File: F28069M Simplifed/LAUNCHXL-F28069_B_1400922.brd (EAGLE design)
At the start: 130.6 x 51.1 mm, 54 parts, among them U1 TMS320F28069MPZT, U10 SN74LV4052APW, U11 TS5A3153DCUR, U13 SN74AHC1G32, U14 SN74AHC1G32, U15 TS5A3153DCUR, U16 TS5A23159DGSR, U18 SN74LVC1G04DCKR, U4 SN74AHC1G02DBVR

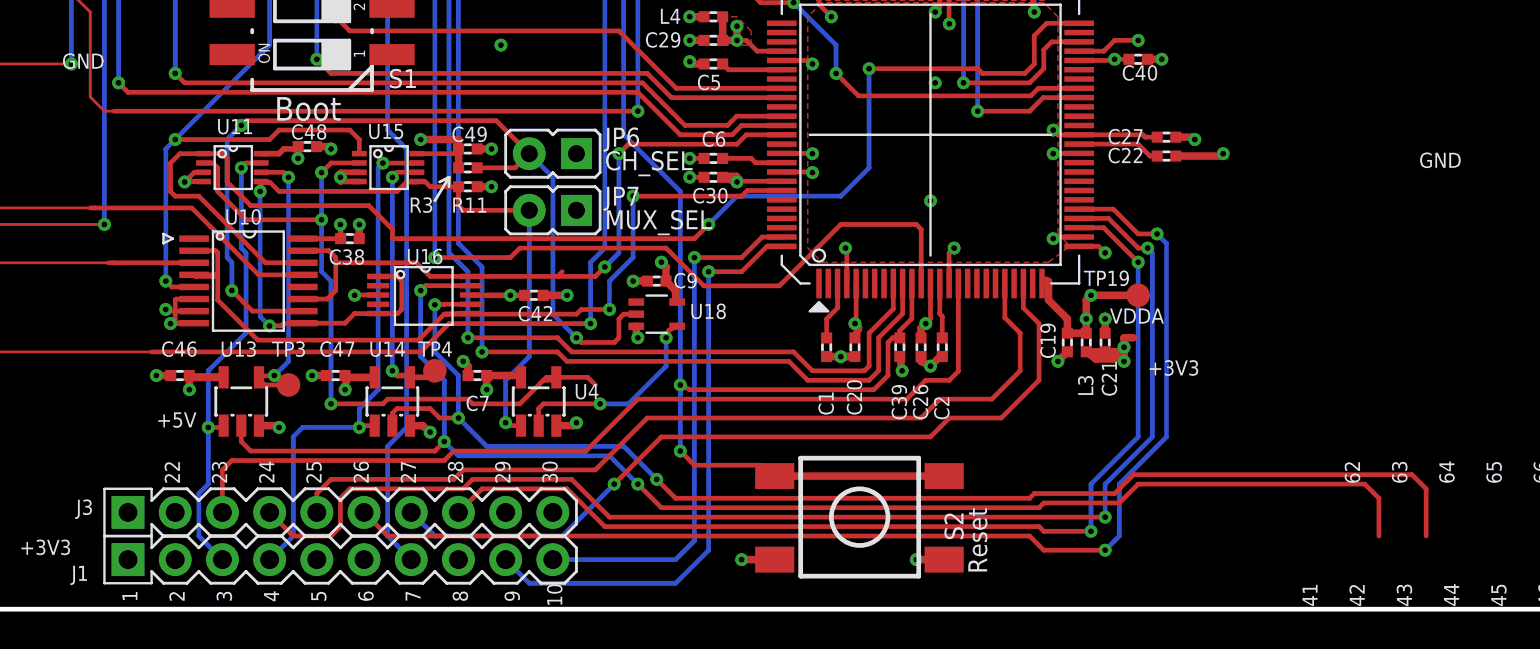
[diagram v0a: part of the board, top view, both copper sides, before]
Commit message: Final simplification of TI's F28069M microcontroller
Decided to remove all muxes and logic gates and make direct connection to GPIO 28 and 29 pins. No need to use their other functionality, serial TX and RX. We believe those serial lines are not involved when identifing a motor or flashing the microcontroller. We also decided on just one switch on TRST signal. The state of that line should decide whether code is automatically run on power up or if code is being flashed.
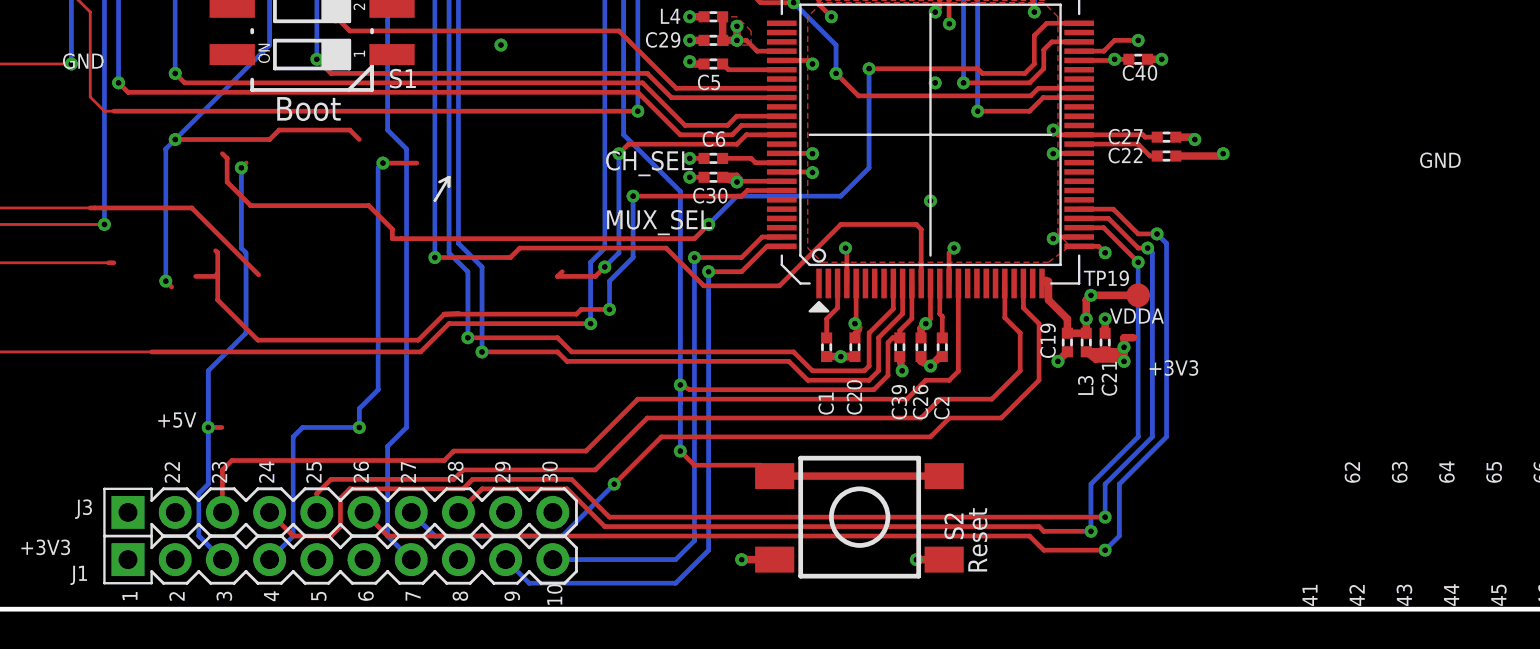
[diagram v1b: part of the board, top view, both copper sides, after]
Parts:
- removed C38, C42, C46, C47, C48, C49, C7, C9: 0.1u, rcl:C0402
- removed JP6, JP7: (no value), jumper:JP1
- removed R11, R3: 10K, rcl:R0402
- removed TP3, TP4: TESTPAD_TPB1,27, RF430FRL152H_EVM_a:TESTPAD_B1,27
- removed U10: SN74LV4052APW, LAUNCHXL-F28027:TSSOP16-PW
- removed U11, U15: TS5A3153DCUR, LAUNCHXL-F28027:TI-DCU8
- removed U13, U14: SN74AHC1G32, LAUNCHXL-F28027:SOT23-5-DBV
- removed U16: TS5A23159DGSR, LAUNCHXL-F28027:TI-DGS10
- removed U18: SN74LVC1G04DCKR, RF430FRL152H_EVM_a:74XX-LITTLE-DE_SC70-5
- removed U4: SN74AHC1G02DBVR, LAUNCHXL-F28027:SOT23-5-DBV
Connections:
- removed net !EN: U11.P$2, U15.P$2, U4.4
- removed net CH_SEL: JP6.2, R3.2, U10.P$10, U18.2
- removed net FAULT_O: TP3.TP, U11.P$6, U13.4
- removed net J7.3: U13.2, U16.P$9
- removed net J7.4: U14.2, U16.P$7
- removed net MUX_SEL: JP7.2, R11.2, U10.P$9, U11.P$5, U15.P$5, U16.P$1, U16.P$5, U4.1
- removed net N$10: S1.5
- removed net N$42: U18.4, U4.2
- removed net OCTW_O: TP4.TP, U14.4, U15.P$6
- net +3V3: no longer C38.1, C42.1, C46.1, C47.1, C48.1, C49.1, C7.1, C9.1, R11.1, R3.1, U10.P$16, U11.P$8, U13.5, U14.5, U15.P$8, U16.P$8, U18.5, U4.5
- net GND: no longer C38.2, C42.2, C46.2, C47.2, C48.2, C49.2, C7.2, C9.2, JP6.1, JP7.1, U10.P$6, U10.P$7, U10.P$8, U11.P$3, U11.P$4, U13.3, U14.3, U15.P$3, U15.P$4, U16.P$3, U18.3, U4.3
- net GPIO15: no longer U10.P$11, U10.P$15, U16.P$10
- net GPIO28: no longer U10.P$14, U11.P$1
- net GPIO29: no longer U10.P$5, U15.P$1
- net GPIO58: no longer U10.P$2, U10.P$4, U16.P$6
- net J1.3: no longer U11.P$7, U13.1
- net J1.4: no longer U14.1, U15.P$7
- net SCI_RX: no longer U10.P$13
- net SCI_TX: no longer U10.P$3
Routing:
- net J7.3: track 78.3 -> 0.00 mm, vias 3 -> 0
- net J7.4: track 70.4 -> 0.00 mm, vias 3 -> 0
- net CH_SEL: track 48.5 -> 0.00 mm, vias 3 -> 0
- net MUX_SEL: track 47.8 -> 0.00 mm, vias 3 -> 0
- net !EN: track 39.0 -> 0.00 mm, vias 3 -> 0
- net +3V3: track 40.0 -> 11.5 mm, vias 15 -> 6
- net GND: track 63.8 -> 39.4 mm, vias 49 -> 32
- net GPIO15: track 36.6 -> 18.7 mm
- net FAULT_O: track 15.3 -> 0.00 mm, vias 2 -> 0
- net OCTW_O: track 14.9 -> 0.00 mm, vias 2 -> 0
- net GPIO28: track 71.3 -> 58.1 mm
- net N$42: track 11.2 -> 0.00 mm, vias 2 -> 0
- net SCI_TX: track 18.3 -> 14.0 mm
- net GPIO58: track 45.3 -> 42.2 mm
- net SCI_RX: track 26.6 -> 24.3 mm
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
